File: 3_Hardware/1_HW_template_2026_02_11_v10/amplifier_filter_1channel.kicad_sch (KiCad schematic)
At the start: 6 parts, among them U3 MCP6002/MCP6272

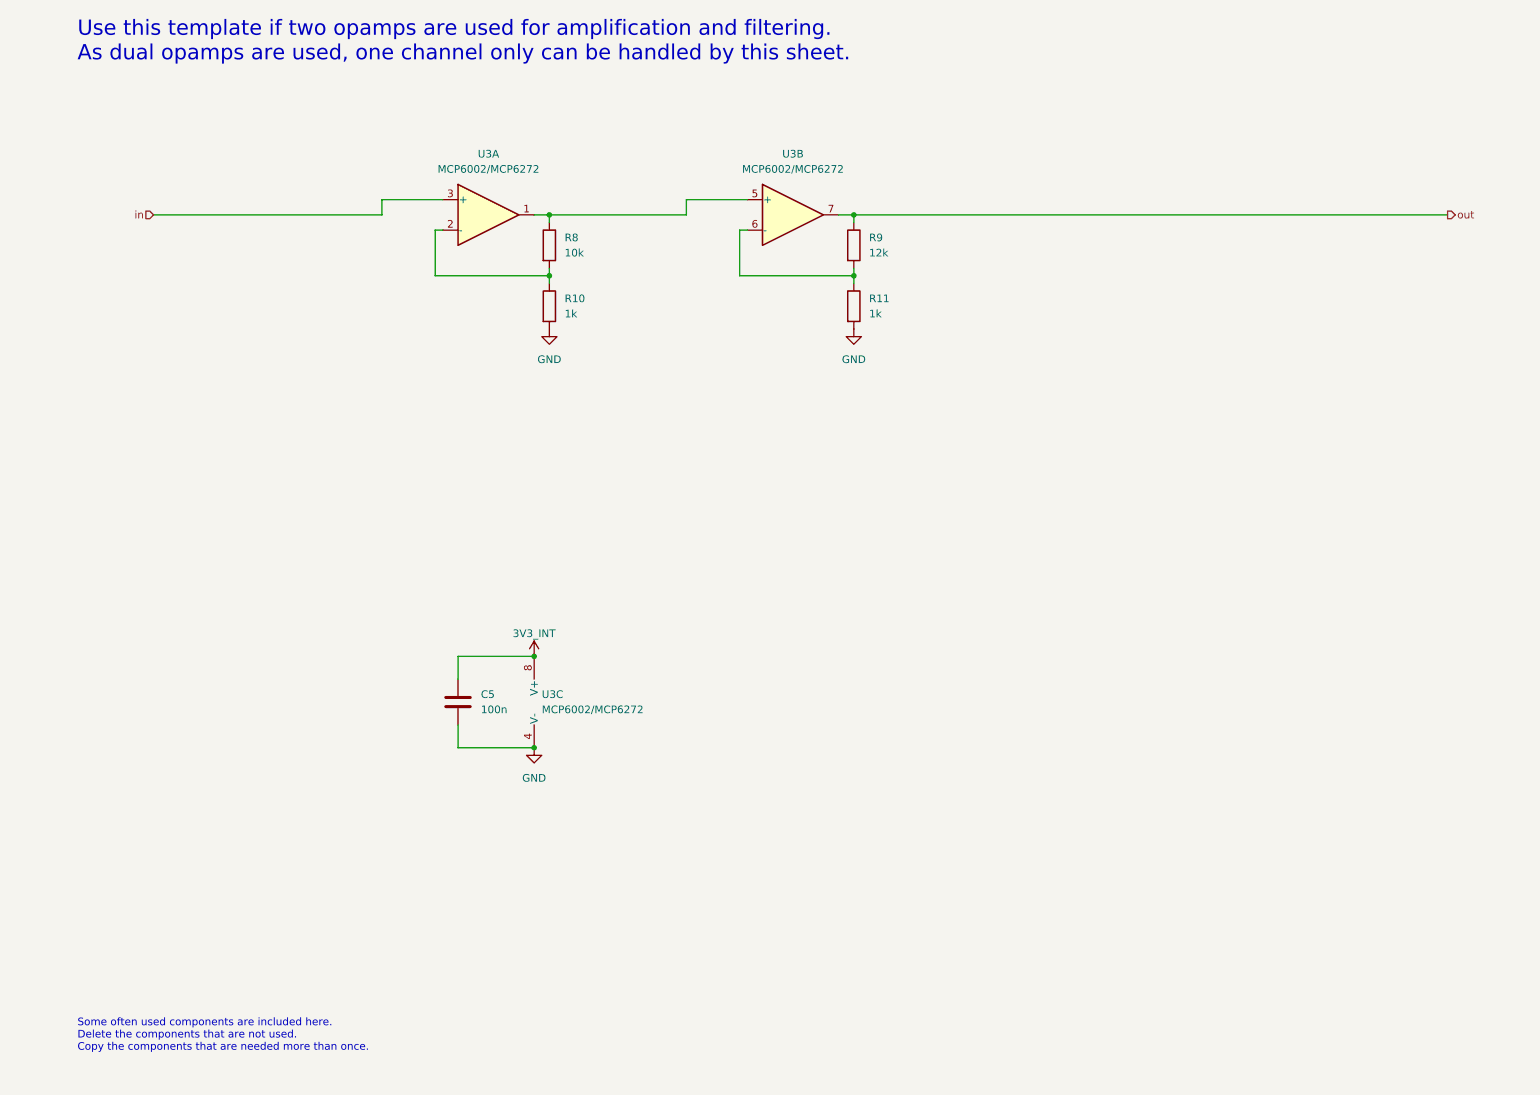
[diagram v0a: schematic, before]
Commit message: first analog circuitry implemented in kicad
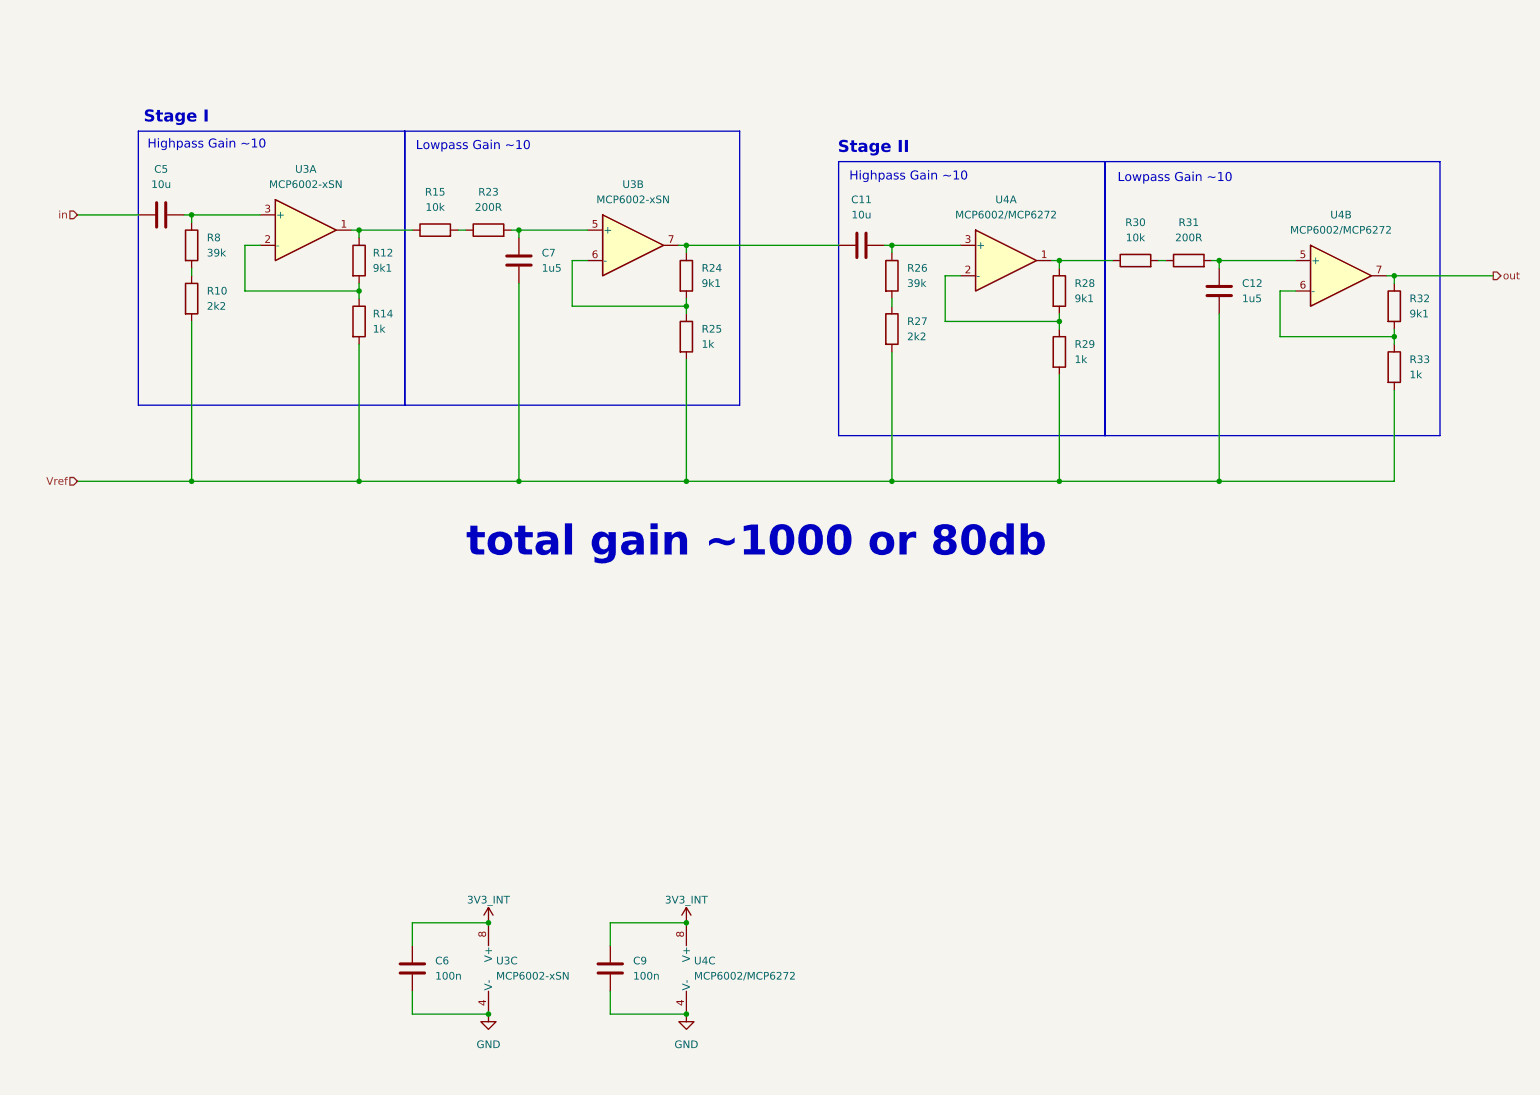
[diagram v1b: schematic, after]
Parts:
- removed R11: 1k, Resistor_SMD:R_0805_2012Metric_Pad1.20x1.40mm_HandSolder, symbol Device:R
- removed R9: 12k, Resistor_SMD:R_0805_2012Metric_Pad1.20x1.40mm_HandSolder, symbol Device:R
- added C11, C5: 10u, Capacitor_SMD:C_0805_2012Metric_Pad1.18x1.45mm_HandSolder, symbol Device:C
- added C12, C7: 1u5, Capacitor_SMD:C_0805_2012Metric_Pad1.18x1.45mm_HandSolder, symbol Device:C
- added C6: 100n, Capacitor_SMD:C_0805_2012Metric_Pad1.18x1.45mm_HandSolder, symbol Device:C
- added R12, R24, R28, R32: 9k1, Resistor_SMD:R_0805_2012Metric_Pad1.20x1.40mm_HandSolder, symbol Device:R
- added R14, R25, R29, R33: 1k, Resistor_SMD:R_0805_2012Metric_Pad1.20x1.40mm_HandSolder, symbol Device:R
- added R15, R30: 10k, Resistor_SMD:R_0805_2012Metric_Pad1.20x1.40mm_HandSolder, symbol Device:R
- added R23, R31: 200R, Resistor_SMD:R_0805_2012Metric_Pad1.20x1.40mm_HandSolder, symbol Device:R
- added R26: 39k, Resistor_SMD:R_0805_2012Metric_Pad1.20x1.40mm_HandSolder, symbol Device:R
- added R27: 2k2, Resistor_SMD:R_0805_2012Metric_Pad1.20x1.40mm_HandSolder, symbol Device:R
- added U3: MCP6002-xSN, Package_SO:SOIC-8_3.9x4.9mm_P1.27mm, symbol Amplifier_Operational:MCP6002-xSN
- R10: value 1k -> 2k2
- R8: value 10k -> 39k
- renumbered C5 to C9, U3 to U4
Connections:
- net 3V3_INT: now also C6.1, U3.8 (V+)
- net GND: now also C6.2, U3.4 (V-); no longer R10.2
- net in: now also C5.1; no longer U4.3 (+)
- net out: now also R32.1
- net at R10.1, R8.2: no longer U4.2 (-)
- net at U4.6 (-): now also R32.2, R33.1
- new net: C7.2, R23.2, U3.5 (+)
- new net: R12.2, R14.1, U3.2 (-)
- new net: C11.2, R26.1, U4.3 (+)
- new net: R26.2, R27.1
- new net: R28.1, R30.1, U4.1
- new net: R30.2, R31.1
- new net: C12.2, R31.2, U4.5 (+)
- new net: C5.2, R8.1, U3.3 (+)
- new net: R28.2, R29.1, U4.2 (-)
- new net: R15.2, R23.1
- new net: C11.1, R24.1, U3.7
- new net: R24.2, R25.1, U3.6 (-)
- new net: R12.1, R15.1, U3.1
- new net Vref: C12.1, C7.1, R10.2, R14.2, R25.2, R27.2, R29.2, R33.2
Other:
- note added: "Highpass Gain ~10"
- note added: "Lowpass Gain ~10"
- note added: "Stage I"
- note added: "Stage II"
- note added: "total gain ~1000 or 80db"
- note removed: "Some often used components are included here. Delete the components that are not used. Copy the components that are needed more than once."
- note removed: "Use this template if two opamps are used for amplification and filtering. As dual opamps are used, one channel only can be handled by this sheet."
- moved on the sheet: C9, U4A, U4B, U4C

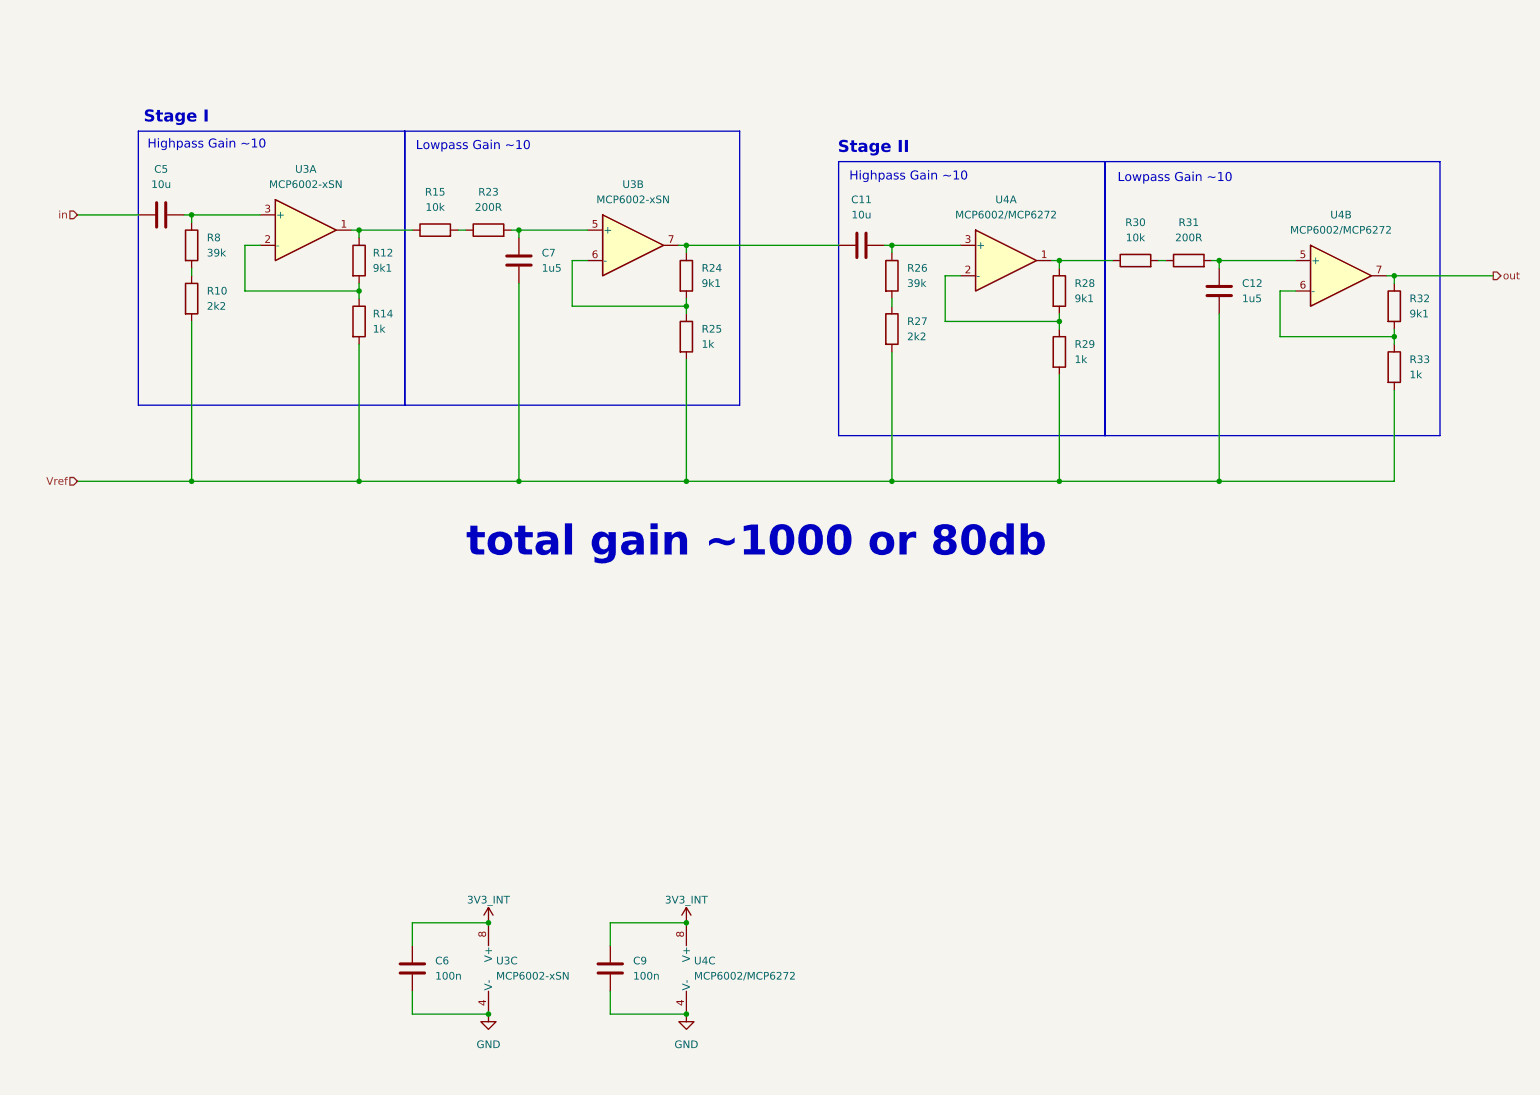
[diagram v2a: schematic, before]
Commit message: finalize main feature
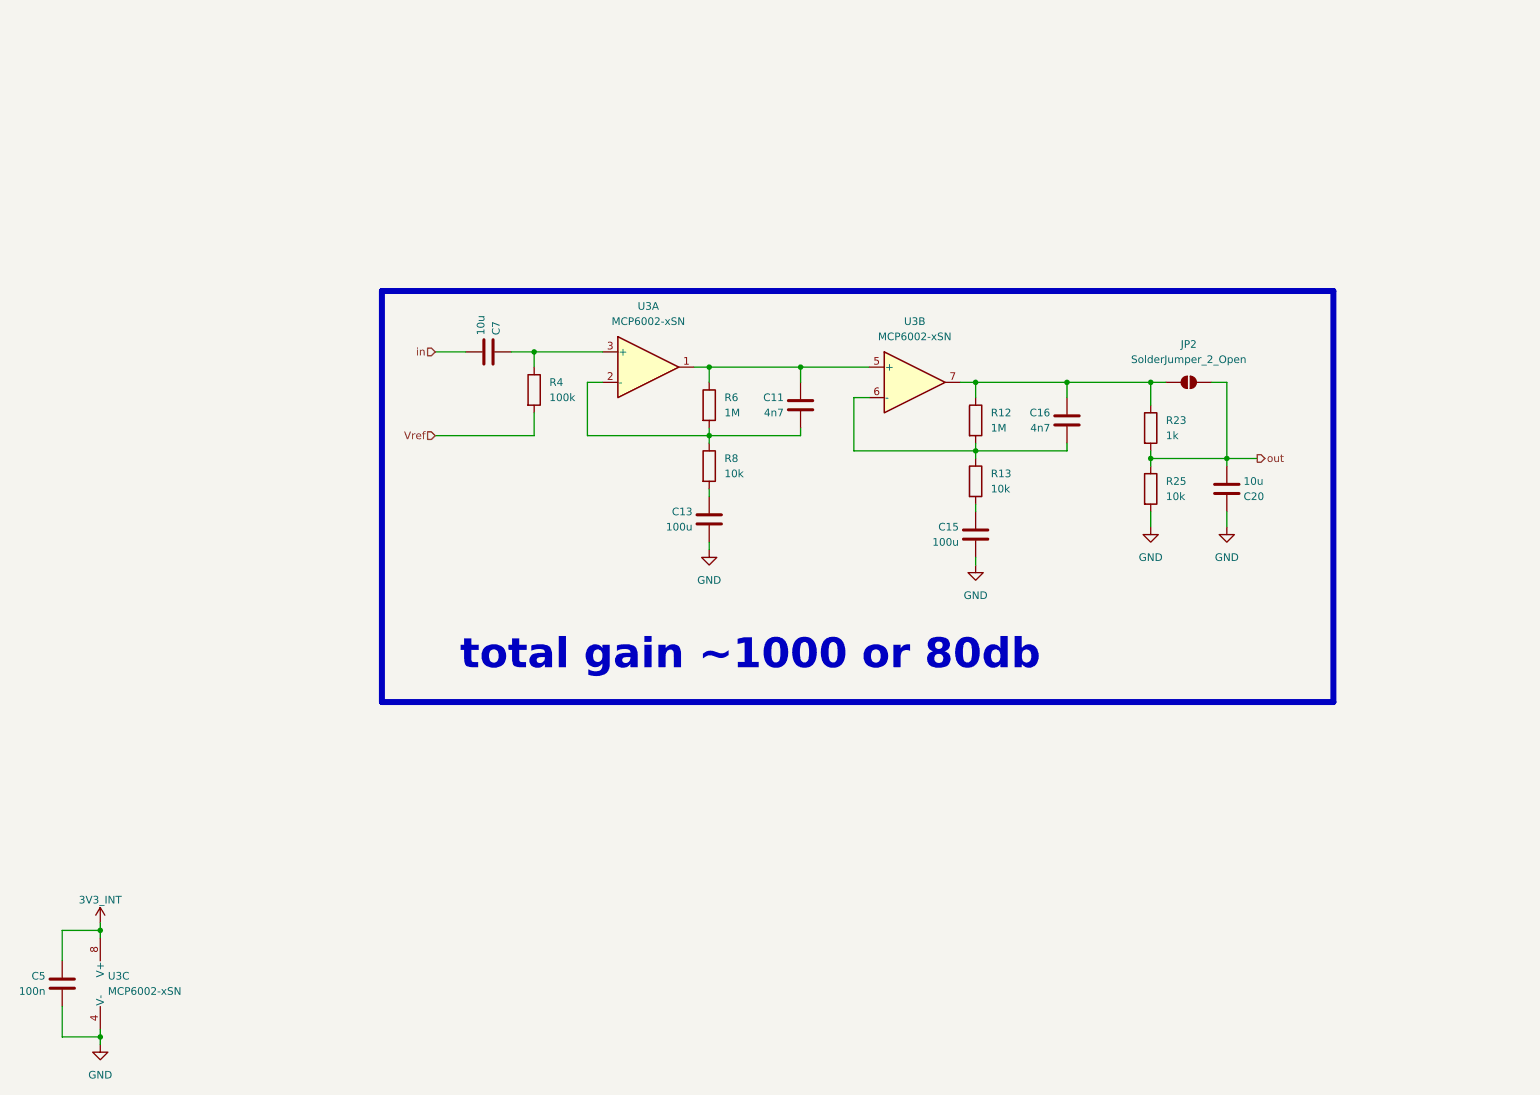
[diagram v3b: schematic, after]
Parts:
- removed C12: 1u5, Capacitor_SMD:C_0805_2012Metric_Pad1.18x1.45mm_HandSolder, symbol Device:C
- removed C6, C9: 100n, Capacitor_SMD:C_0805_2012Metric_Pad1.18x1.45mm_HandSolder, symbol Device:C
- removed R10, R27: 2k2, Resistor_SMD:R_0805_2012Metric_Pad1.20x1.40mm_HandSolder, symbol Device:R
- removed R14, R29, R33: 1k, Resistor_SMD:R_0805_2012Metric_Pad1.20x1.40mm_HandSolder, symbol Device:R
- removed R15, R30: 10k, Resistor_SMD:R_0805_2012Metric_Pad1.20x1.40mm_HandSolder, symbol Device:R
- removed R24, R28, R32: 9k1, Resistor_SMD:R_0805_2012Metric_Pad1.20x1.40mm_HandSolder, symbol Device:R
- removed R26: 39k, Resistor_SMD:R_0805_2012Metric_Pad1.20x1.40mm_HandSolder, symbol Device:R
- removed R31: 200R, Resistor_SMD:R_0805_2012Metric_Pad1.20x1.40mm_HandSolder, symbol Device:R
- removed U4: MCP6002/MCP6272, Package_SO:SOIC-8_3.9x4.9mm_P1.27mm, symbol Amplifier_Operational:MCP6002-xSN
- added C13, C15: 100u, Capacitor_SMD:C_0805_2012Metric_Pad1.18x1.45mm_HandSolder, symbol Device:C
- added C16: 4n7, Capacitor_SMD:C_0805_2012Metric_Pad1.18x1.45mm_HandSolder, symbol Device:C
- added C20: 10u, Capacitor_SMD:C_0805_2012Metric_Pad1.18x1.45mm_HandSolder, symbol Device:C
- added JP2: SolderJumper_2_Open, symbol Jumper:SolderJumper_2_Open
- added R13: 10k, Resistor_SMD:R_0805_2012Metric_Pad1.20x1.40mm_HandSolder, symbol Device:R
- added R4: 100k, Resistor_SMD:R_0805_2012Metric_Pad1.20x1.40mm_HandSolder, symbol Device:R
- added R6: 1M, Resistor_SMD:R_0805_2012Metric_Pad1.20x1.40mm_HandSolder, symbol Device:R
- C11: value 10u -> 4n7
- C5: value 10u -> 100n
- C7: value 1u5 -> 10u
- R12: value 9k1 -> 1M
- R23: value 200R -> 1k
- R25: value 1k -> 10k
- R8: value 39k -> 10k
- U3: footprint Package_SO:SOIC-8_3.9x4.9mm_P1.27mm -> (none)
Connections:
- net 3V3_INT: now also C5.1
- net GND: now also C5.2, R25.2, C13.2, C15.2, C20.1
- net Vref: now also R4.2; no longer C7.1, R25.2
- net in: now also C7.2; no longer C5.1
- net out: now also R23.2, R25.1, C20.2, JP2.2 (B)
- net at R12.2: now also U3.6 (-), C16.2, R13.1; no longer U3.2 (-)
- net at C11.2: now also R8.1, U3.2 (-), R6.2
- net at R23.1: now also R12.1, U3.7, C16.1, JP2.1 (A)
- net at R8.2: now also C13.1
- net at C11.1: now also U3.1, U3.5 (+), R6.1; no longer U3.7
- new net: C15.1, R13.2
- new net: C7.1, R4.1, U3.3 (+)
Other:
- note removed: "Highpass Gain ~10"
- note removed: "Lowpass Gain ~10"
- note removed: "Stage I"
- note removed: "Stage II"

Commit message: layout template
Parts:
- C1: renamed from C5; footprint Capacitor_SMD:C_0805_2012Metric_Pad1.18x1.45mm_HandSolder -> Capacitor_SMD:C_0603_1608Metric_Pad1.08x0.95mm_HandSolder
- C2: renamed from C7; footprint Capacitor_SMD:C_0805_2012Metric_Pad1.18x1.45mm_HandSolder -> Capacitor_SMD:C_0603_1608Metric_Pad1.08x0.95mm_HandSolder
- C3: renamed from C13; footprint Capacitor_SMD:C_0805_2012Metric_Pad1.18x1.45mm_HandSolder -> Capacitor_SMD:C_1210_3225Metric_Pad1.33x2.70mm_HandSolder
- C4: renamed from C11; footprint Capacitor_SMD:C_0805_2012Metric_Pad1.18x1.45mm_HandSolder -> Capacitor_SMD:C_0603_1608Metric_Pad1.08x0.95mm_HandSolder
- C5: renamed from C15; footprint Capacitor_SMD:C_0805_2012Metric_Pad1.18x1.45mm_HandSolder -> Capacitor_SMD:C_1210_3225Metric_Pad1.33x2.70mm_HandSolder
- C6: renamed from C16; footprint Capacitor_SMD:C_0805_2012Metric_Pad1.18x1.45mm_HandSolder -> Capacitor_SMD:C_0603_1608Metric_Pad1.08x0.95mm_HandSolder
- C7: renamed from C20; footprint Capacitor_SMD:C_0805_2012Metric_Pad1.18x1.45mm_HandSolder -> Capacitor_SMD:C_0603_1608Metric_Pad1.08x0.95mm_HandSolder
- JP1: renamed from JP2; footprint (none) -> Jumper:SolderJumper-2_P1.3mm_Open_RoundedPad1.0x1.5mm
- R1: renamed from R4; footprint Resistor_SMD:R_0805_2012Metric_Pad1.20x1.40mm_HandSolder -> Resistor_SMD:R_0603_1608Metric_Pad0.98x0.95mm_HandSolder
- R2: renamed from R6; footprint Resistor_SMD:R_0805_2012Metric_Pad1.20x1.40mm_HandSolder -> Resistor_SMD:R_0603_1608Metric_Pad0.98x0.95mm_HandSolder
- R3: renamed from R8; footprint Resistor_SMD:R_0805_2012Metric_Pad1.20x1.40mm_HandSolder -> Resistor_SMD:R_0603_1608Metric_Pad0.98x0.95mm_HandSolder
- R4: renamed from R12; footprint Resistor_SMD:R_0805_2012Metric_Pad1.20x1.40mm_HandSolder -> Resistor_SMD:R_0603_1608Metric_Pad0.98x0.95mm_HandSolder
- R5: renamed from R13; footprint Resistor_SMD:R_0805_2012Metric_Pad1.20x1.40mm_HandSolder -> Resistor_SMD:R_0603_1608Metric_Pad0.98x0.95mm_HandSolder
- R6: renamed from R23; footprint Resistor_SMD:R_0805_2012Metric_Pad1.20x1.40mm_HandSolder -> Resistor_SMD:R_0603_1608Metric_Pad0.98x0.95mm_HandSolder
- R7: renamed from R25; footprint Resistor_SMD:R_0805_2012Metric_Pad1.20x1.40mm_HandSolder -> Resistor_SMD:R_0603_1608Metric_Pad0.98x0.95mm_HandSolder
- U1: renamed from U3; footprint (none) -> Package_SO:SOIC-8_3.9x4.9mm_P1.27mm
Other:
- note added: "total gain ~10000 or 80db"
- note removed: "total gain ~1000 or 80db"

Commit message: fixed footprints
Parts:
- C3, C5: footprint Capacitor_SMD:C_1210_3225Metric_Pad1.33x2.70mm_HandSolder -> Capacitor_SMD:C_1206_3216Metric_Pad1.33x1.80mm_HandSolder
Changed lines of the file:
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@@
 			)
 		)
-		(property "Footprint" "Capacitor_SMD:C_1210_3225Metric_Pad1.33x2.70mm_HandSolder"
+		(property "Footprint" "Capacitor_SMD:C_1206_3216Metric_Pad1.33x1.80mm_HandSolder"
 			(at 174.2948 107.95 0)
 			(effects
@@
 			)
 		)
-		(property "Footprint" "Capacitor_SMD:C_1210_3225Metric_Pad1.33x2.70mm_HandSolder"
+		(property "Footprint" "Capacitor_SMD:C_1206_3216Metric_Pad1.33x1.80mm_HandSolder"
 			(at 129.8448 105.41 0)
 			(effects

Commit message: pcb fix
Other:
- note added: "correction: 100k"
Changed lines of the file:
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@@
+		)
+	)
+	(text "correction: 100k"
+		(exclude_from_sim no)
+		(at 191.77 88.392 0)
+		(effects
+			(font
+				(size 1.27 1.27)
+				(color 255 0 0 1)
+			)
 		)
 	)
